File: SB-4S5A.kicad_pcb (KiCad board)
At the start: 4 copper layers, 110 x 30 mm, 39 parts, among them J1 CONN_01X06, Q1 CSD17308Q3, Q2 CSD17308Q3, Q3 2N7002, U1 bq40z50-r2

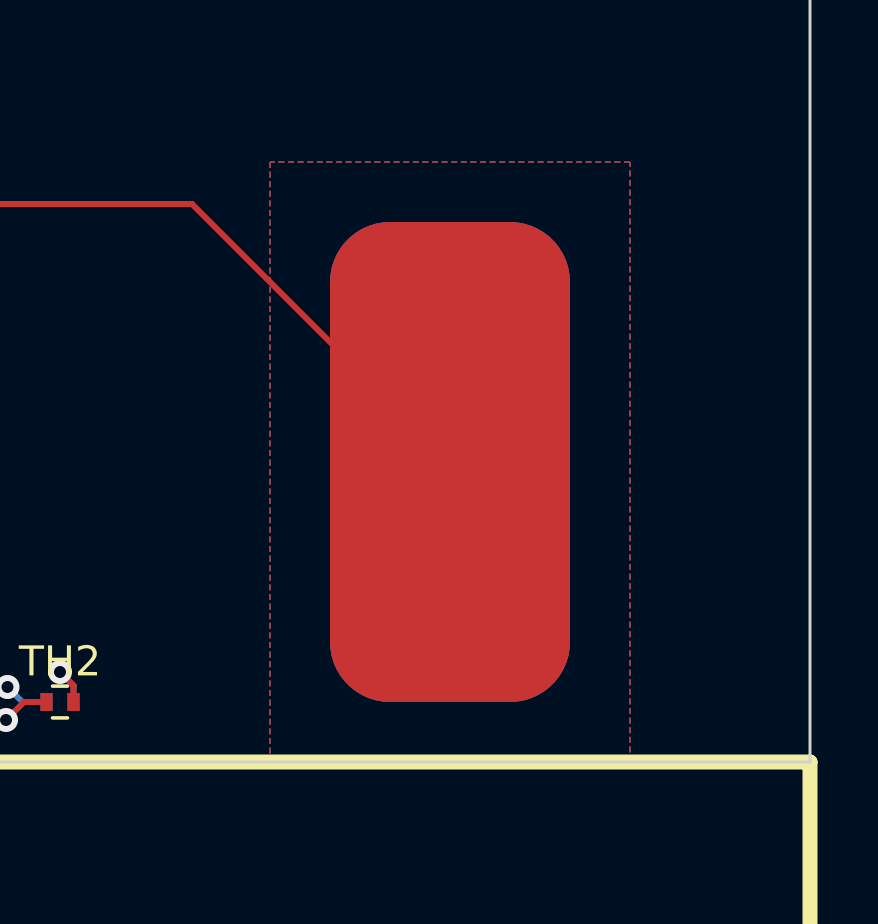
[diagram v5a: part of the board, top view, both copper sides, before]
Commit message: Fix missing vias on VC2A
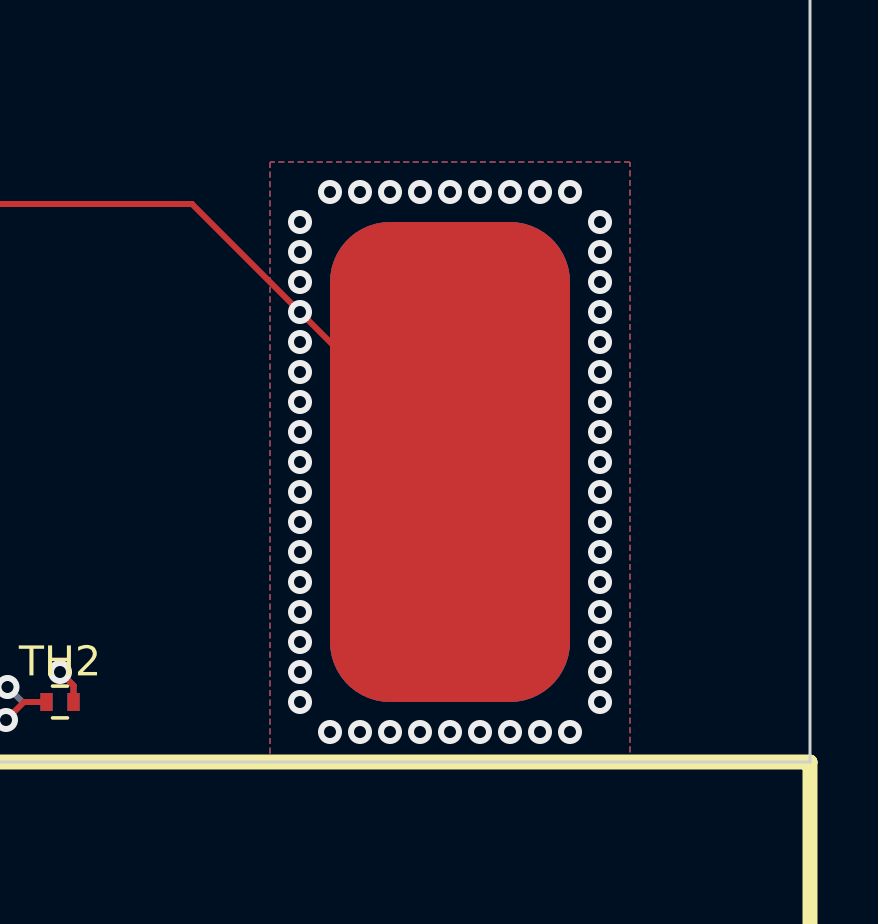
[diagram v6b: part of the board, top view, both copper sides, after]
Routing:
- net /_VCC_: track 43.1 -> 42.0 mm
- net /VC2A: vias 0 -> 51
- net (no net): vias 0 -> 1
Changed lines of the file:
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@@
-(kicad_pcb (version 20170123) (host pcbnew no-vcs-found-ee43728~59~ubuntu16.04.1)
+(kicad_pcb (version 20170123) (host pcbnew no-vcs-found-db3491f~59~ubuntu16.04.1)
   (general
     (thickness 1.6)
     (drawings 4)
-    (tracks 345)
+    (tracks 396)
     (zones 0)
     (modules 39)
@@
   (layers
     (0 F.Cu signal)
-    (1 In1.Cu mixed hide)
+    (1 In1.Cu mixed)
     (2 In2.Cu mixed)
     (31 B.Cu signal)
@@
     (47 F.CrtYd user)
     (48 B.Fab user)
-    (49 F.Fab user hide)
+    (49 F.Fab user)
   )
   (setup
@@
     (pad_to_mask_clearance 0)
     (aux_axis_origin 0 0)
-    (visible_elements FFFFFF7F)
+    (visible_elements FFFFFFFF)
     (pcbplotparams
       (layerselection 0x00030_ffffffff)
@@
   (gr_line (start 70 60) (end 180 60) (angle 90) (layer Edge.Cuts) (width 0.1))
   (gr_line (start 70 90) (end 70 60) (angle 90) (layer Edge.Cuts) (width 0.1))
+  (via (at 163 75) (size 0.8) (drill 0.4) (layers F.Cu B.Cu) (net 0))
   (segment (start 155.45 88) (end 155.45 87.45) (width 0.2) (layer B.Cu) (net 1) (status 10))
   (segment (start 155.45 87.45) (end 155 87) (width 0.2) (layer B.Cu) (net 1))
@@
   (segment (start 102.2 70.75) (end 101.05 70.75) (width 0.2) (layer F.Cu) (net 10) (status 30))
   (segment (start 101.05 70.75) (end 101 70.8) (width 0.2) (layer F.Cu) (net 10) (status 30))
+  (via (at 163 88) (size 0.8) (drill 0.4) (layers F.Cu B.Cu) (net 11))
+  (via (at 163 87) (size 0.8) (drill 0.4) (layers F.Cu B.Cu) (net 11))
+  (via (at 163 86) (size 0.8) (drill 0.4) (layers F.Cu B.Cu) (net 11))
+  (via (at 163 85) (size 0.8) (drill 0.4) (layers F.Cu B.Cu) (net 11))
+  (via (at 163 84) (size 0.8) (drill 0.4) (layers F.Cu B.Cu) (net 11))
+  (via (at 163 83) (size 0.8) (drill 0.4) (layers F.Cu B.Cu) (net 11))
+  (via (at 163 82) (size 0.8) (drill 0.4) (layers F.Cu B.Cu) (net 11))
+  (via (at 163 81) (size 0.8) (drill 0.4) (layers F.Cu B.Cu) (net 11))
+  (via (at 163 80) (size 0.8) (drill 0.4) (layers F.Cu B.Cu) (net 11))
+  (via (at 163 79) (size 0.8) (drill 0.4) (layers F.Cu B.Cu) (net 11))
+  (via (at 163 78) (size 0.8) (drill 0.4) (layers F.Cu B.Cu) (net 11))
+  (via (at 163 77) (size 0.8) (drill 0.4) (layers F.Cu B.Cu) (net 11))
+  (via (at 163 76) (size 0.8) (drill 0.4) (layers F.Cu B.Cu) (net 11))
+  (via (at 163 74) (size 0.8) (drill 0.4) (layers F.Cu B.Cu) (net 11))
+  (via (at 163 73) (size 0.8) (drill 0.4) (layers F.Cu B.Cu) (net 11))
+  (via (at 163 72) (size 0.8) (drill 0.4) (layers F.Cu B.Cu) (net 11))
+  (via (at 164 71) (size 0.8) (drill 0.4) (layers F.Cu B.Cu) (net 11))
+  (via (at 165 71) (size 0.8) (drill 0.4) (layers F.Cu B.Cu) (net 11))
+  (via (at 166 71) (size 0.8) (drill 0.4) (layers F.Cu B.Cu) (net 11))
+  (via (at 167 71) (size 0.8) (drill 0.4) (layers F.Cu B.Cu) (net 11))
+  (via (at 168 71) (size 0.8) (drill 0.4) (layers F.Cu B.Cu) (net 11))
+  (via (at 169 71) (size 0.8) (drill 0.4) (layers F.Cu B.Cu) (net 11))
+  (via (at 170 71) (size 0.8) (drill 0.4) (layers F.Cu B.Cu) (net 11))
+  (via (at 171 71) (size 0.8) (drill 0.4) (layers F.Cu B.Cu) (net 11))
+  (via (at 172 71) (size 0.8) (drill 0.4) (layers F.Cu B.Cu) (net 11))
+  (via (at 173 72) (size 0.8) (drill 0.4) (layers F.Cu B.Cu) (net 11))
+  (via (at 173 73) (size 0.8) (drill 0.4) (layers F.Cu B.Cu) (net 11))
+  (via (at 173 74) (size 0.8) (drill 0.4) (layers F.Cu B.Cu) (net 11))
+  (via (at 173 75) (size 0.8) (drill 0.4) (layers F.Cu B.Cu) (net 11))
+  (via (at 173 76) (size 0.8) (drill 0.4) (layers F.Cu B.Cu) (net 11))
+  (via (at 173 77) (size 0.8) (drill 0.4) (layers F.Cu B.Cu) (net 11))
+  (via (at 173 78) (size 0.8) (drill 0.4) (layers F.Cu B.Cu) (net 11))
+  (via (at 173 79) (size 0.8) (drill 0.4) (layers F.Cu B.Cu) (net 11))
+  (via (at 173 80) (size 0.8) (drill 0.4) (layers F.Cu B.Cu) (net 11))
+  (via (at 173 81) (size 0.8) (drill 0.4) (layers F.Cu B.Cu) (net 11))
+  (via (at 173 82) (size 0.8) (drill 0.4) (layers F.Cu B.Cu) (net 11))
+  (via (at 173 83) (size 0.8) (drill 0.4) (layers F.Cu B.Cu) (net 11))
+  (via (at 173 84) (size 0.8) (drill 0.4) (layers F.Cu B.Cu) (net 11))
+  (via (at 173 85) (size 0.8) (drill 0.4) (layers F.Cu B.Cu) (net 11))
+  (via (at 173 86) (size 0.8) (drill 0.4) (layers F.Cu B.Cu) (net 11))
+  (via (at 173 87) (size 0.8) (drill 0.4) (layers F.Cu B.Cu) (net 11))
+  (via (at 173 88) (size 0.8) (drill 0.4) (layers F.Cu B.Cu) (net 11))
+  (via (at 172 89) (size 0.8) (drill 0.4) (layers F.Cu B.Cu) (net 11))
+  (via (at 171 89) (size 0.8) (drill 0.4) (layers F.Cu B.Cu) (net 11))
+  (via (at 170 89) (size 0.8) (drill 0.4) (layers F.Cu B.Cu) (net 11))
+  (via (at 169 89) (size 0.8) (drill 0.4) (layers F.Cu B.Cu) (net 11))
+  (via (at 168 89) (size 0.8) (drill 0.4) (layers F.Cu B.Cu) (net 11))
+  (via (at 167 89) (size 0.8) (drill 0.4) (layers F.Cu B.Cu) (net 11))
+  (via (at 166 89) (size 0.8) (drill 0.4) (layers F.Cu B.Cu) (net 11))
+  (via (at 165 89) (size 0.8) (drill 0.4) (layers F.Cu B.Cu) (net 11))
+  (via (at 164 89) (size 0.8) (drill 0.4) (layers F.Cu B.Cu) (net 11))
   (segment (start 108.6 71.4) (end 159.4 71.4) (width 0.2) (layer F.Cu) (net 11))
   (segment (start 159.4 71.4) (end 168 80) (width 0.2) (layer F.Cu) (net 11))
@@
   (segment (start 76.8 73.8) (end 76.2 74.4) (width 0.2) (layer F.Cu) (net 29))
   (via (at 76.2 74.4) (size 0.8) (drill 0.4) (layers F.Cu B.Cu) (net 29))
+  (segment (start 77.4 72.6) (end 76.834315 72.6) (width 0.2) (layer In2.Cu) (net 30))
+  (segment (start 76.834315 72.6) (end 76.516801 72.917514) (width 0.2) (layer In2.Cu) (net 30))
+  (segment (start 76.860001 74.716801) (end 76.56001 75.016792) (width 0.2) (layer In2.Cu) (net 30))
+  (segment (start 76.516801 72.917514) (end 76.516801 73.739999) (width 0.2) (layer In2.Cu) (net 30))
+  (segment (start 76.516801 73.739999) (end 76.860001 74.083199) (width 0.2) (layer In2.Cu) (net 30))
+  (segment (start 76.860001 74.083199) (end 76.860001 74.716801) (width 0.2) (layer In2.Cu) (net 30))
+  (segment (start 76.56001 75.016792) (end 76.56001 84.939999) (width 0.2) (layer In2.Cu) (net 30))
+  (segment (start 76.56001 84.939999) (end 77.6 85.979989) (width 0.2) (layer In2.Cu) (net 30))
+  (segment (start 77.6 85.979989) (end 98.820011 85.979989) (width 0.2) (layer In2.Cu) (net 30))
+  (segment (start 98.820011 85.979989) (end 99.8 85) (width 0.2) (layer In2.Cu) (net 30))
   (segment (start 100.8 83.15) (end 100.8 84) (width 0.2) (layer F.Cu) (net 30))
   (segment (start 100.8 84) (end 99.8 85) (width 0.2) (layer F.Cu) (net 30))
   (segment (start 99.9 82.75) (end 100.4 82.75) (width 0.2) (layer F.Cu) (net 30))
   (segment (start 100.4 82.75) (end 100.8 83.15) (width 0.2) (layer F.Cu) (net 30))
-  (segment (start 96.8 85.979989) (end 98.820011 85.979989) (width 0.2) (layer In2.Cu) (net 30))
-  (segment (start 98.820011 85.979989) (end 99.8 85) (width 0.2) (layer In2.Cu) (net 30))
   (via (at 99.8 85) (size 0.8) (drill 0.4) (layers F.Cu B.Cu) (net 30))
-  (segment (start 77.6 85.979989) (end 96.8 85.979989) (width 0.2) (layer In2.Cu) (net 30))
-  (segment (start 76.56001 84.939999) (end 77.6 85.979989) (width 0.2) (layer In2.Cu) (net 30))
-  (segment (start 77.4 72.6) (end 76.834315 72.6) (width 0.2) (layer In2.Cu) (net 30))
-  (segment (start 76.860001 74.083199) (end 76.860001 74.716801) (width 0.2) (layer In2.Cu) (net 30))
-  (segment (start 76.834315 72.6) (end 75.694316 73.739999) (width 0.2) (layer In2.Cu) (net 30))
-  (segment (start 75.694316 73.739999) (end 76.516801 73.739999) (width 0.2) (layer In2.Cu) (net 30))
-  (segment (start 76.516801 73.739999) (end 76.860001 74.083199) (width 0.2) (layer In2.Cu) (net 30))
-  (segment (start 76.56001 75.016792) (end 76.56001 84.939999) (width 0.2) (layer In2.Cu) (net 30))
-  (segment (start 76.860001 74.716801) (end 76.56001 75.016792) (width 0.2) (layer In2.Cu) (net 30))
   (segment (start 76.2 72.5) (end 77.3 72.5) (width 0.2) (layer F.Cu) (net 30))
   (segment (start 77.3 72.5) (end 77.4 72.6) (width 0.2) (layer F.Cu) (net 30))

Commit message: Move kelvin connection for VC3A to the correct place.
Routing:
- net /VC3A: track 19.2 -> 52.8 mm
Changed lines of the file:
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@@
   (segment (start 96.1 81.95) (end 95.6 81.95) (width 0.2) (layer F.Cu) (net 8))
   (segment (start 95.6 81.95) (end 94.8 82.75) (width 0.2) (layer F.Cu) (net 8))
-  (segment (start 101 68.8) (end 99.75 70.05) (width 0.2) (layer F.Cu) (net 9))
-  (segment (start 99.75 70.05) (end 99.75 70.8) (width 0.2) (layer F.Cu) (net 9))
-  (segment (start 105.4 68.8) (end 101 68.8) (width 0.2) (layer F.Cu) (net 9))
-  (segment (start 106.6 70) (end 105.4 68.8) (width 0.2) (layer F.Cu) (net 9))
-  (segment (start 106.6 74.6) (end 106.6 70) (width 0.2) (layer F.Cu) (net 9))
-  (segment (start 108 80) (end 108 76) (width 0.2) (layer F.Cu) (net 9))
-  (segment (start 108 76) (end 106.6 74.6) (width 0.2) (layer F.Cu) (net 9))
+  (segment (start 99.75 70.8) (end 99.75 70.073198) (width 0.2) (layer F.Cu) (net 9))
+  (segment (start 99.75 70.073198) (end 100.883199 68.939999) (width 0.2) (layer F.Cu) (net 9))
+  (segment (start 100.883199 68.939999) (end 105.630869 68.939999) (width 0.2) (layer F.Cu) (net 9))
+  (segment (start 142 71.9) (end 142 80) (width 0.2) (layer F.Cu) (net 9))
+  (segment (start 105.630869 68.939999) (end 108.450879 71.76001) (width 0.2) (layer F.Cu) (net 9))
+  (segment (start 108.450879 71.76001) (end 141.86001 71.76001) (width 0.2) (layer F.Cu) (net 9))
+  (segment (start 141.86001 71.76001) (end 142 71.9) (width 0.2) (layer F.Cu) (net 9))
   (segment (start 80.423198 80) (end 77.2 80) (width 0.2) (layer In2.Cu) (net 10))
   (via (at 77.2 80) (size 0.7) (drill 0.3) (layers F.Cu B.Cu) (net 10))

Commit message: Convert to "KiCad 5.0" format.
Other stuff
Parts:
- added REF**: MountingHole_3.2mm_M3_Pad, Mounting_Holes:MountingHole_3.2mm_M3_Pad, F.Cu at (120.0, 65.0)
- added REF**: MountingHole_3.2mm_M3_Pad, Mounting_Holes:MountingHole_3.2mm_M3_Pad, F.Cu at (165.0, 65.0)
- moved BT2 10.0 mm to (145.0, 90.0)
- moved BT3 10.0 mm to (145.0, 90.0)
- moved TH2 10.0 mm to (145.0, 88.0)
- moved TH3 10.0 mm to (145.0, 88.0)
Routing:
- net /VC3A: track 52.8 -> 19.0 mm
- net Net-(TH2-Pad1): track 70.0 -> 60.0 mm
- net Net-(TH3-Pad1): track 67.4 -> 57.4 mm
- net /VC2A: track 75.5 -> 65.6 mm, vias 51 -> 52
- net (no net): vias 1 -> 0
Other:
- board size 110 x 30 mm -> 100 x 50 mm
- net class Default: clearance 0.16 -> 0.15; trace_width 0.2 -> 0.25
- net class PWR: clearance 0.16 -> 0.15
- rule trace_clearance: 0.16 -> 0.15
- rule trace_min: 0.2 -> 0.15
